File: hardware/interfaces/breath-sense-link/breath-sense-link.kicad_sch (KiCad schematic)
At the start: 5 parts

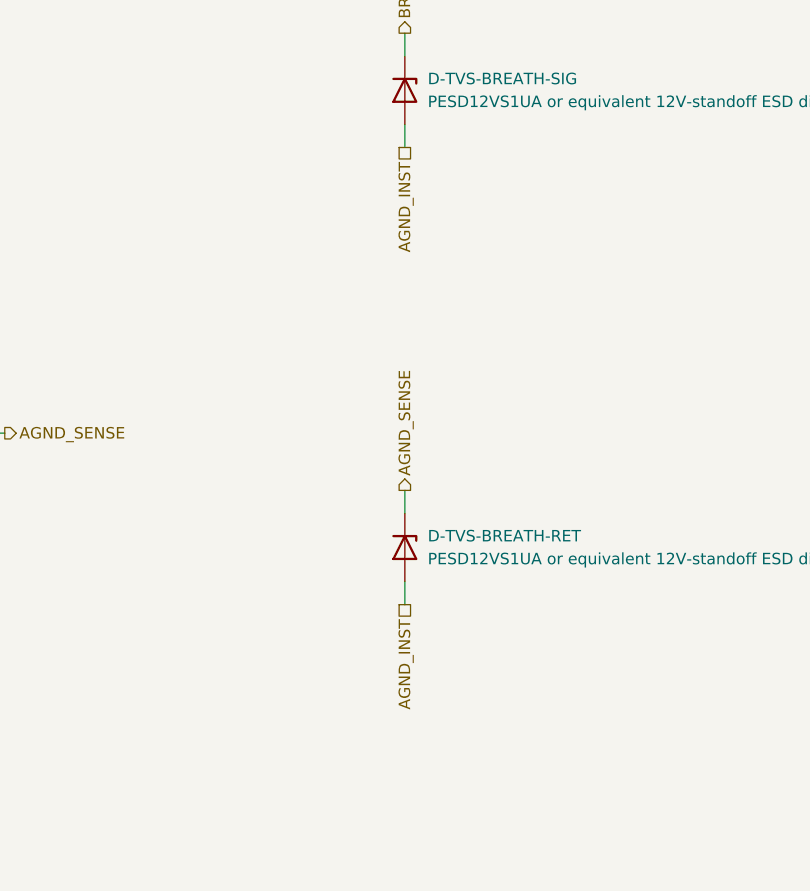
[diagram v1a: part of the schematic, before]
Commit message: Four-layer main-board ground written; breath clamps to the PWR_GND plane
power-entry-instrument.md section 2: layer 2 is the PWR_GND plane under every
SPI/chain/LED trace; AGND_INST is an island under the analog block, tied by
NT-AGND under U-ADC; the breath pair crosses as a pair (AGND_SENSE Kelvin at
the sensor). D-TVS-BREATH anodes move from AGND_INST to PWR_GND (sheet, board,
nets.yaml). dig-gnd-topology stays disputed: its dispute is the MODULE board,
whose layer count is the owner's; a four-layer proposal is recorded on it.

Co-Authored-By: Claude Opus 5.5 <noreply@anthropic.com>
Claude-Session: https://claude.ai/code/session_01LmB4muFXnoLprWX4JzuJ5A
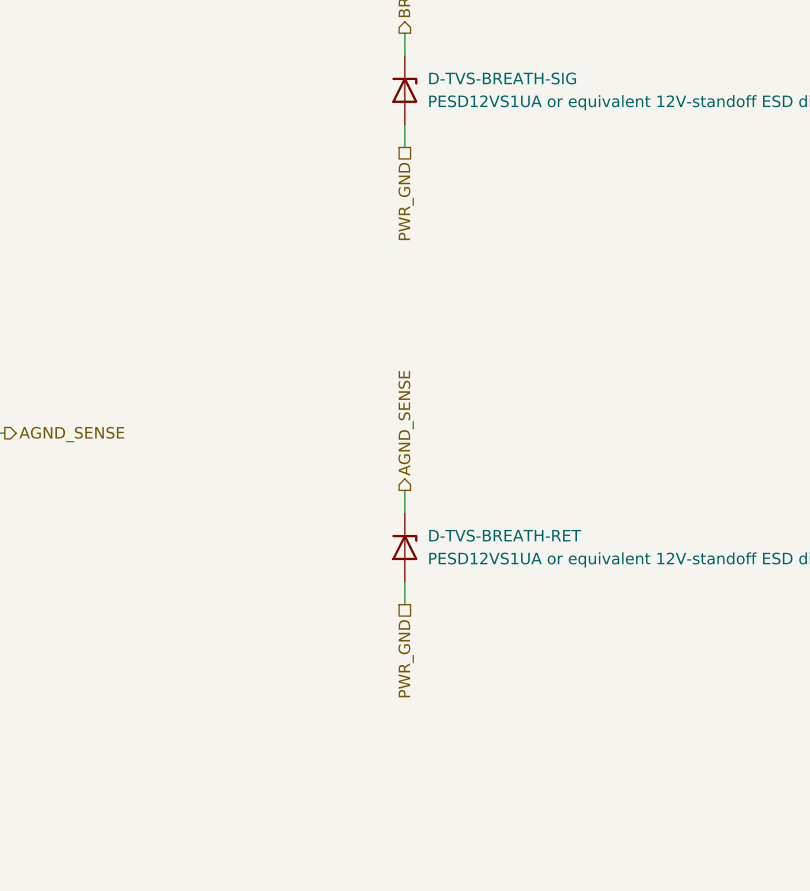
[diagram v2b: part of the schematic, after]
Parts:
- D-TVS-BREATH-RET: Note The second of the pair, on the AGND conductor -> The second of the pair, on the AGND_SENSE conductor. Anode 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
- D-TVS-BREATH-SIG: Note AT THE CONNECTOR, 12 V standoff - above the sensor's full scale so it never conducts in play -> AT THE CONNECTOR, 12 V standoff - above the sensor's full scale so it never conducts in play. Anode to the PWR_GND plane at J-UMB, never to the analog island
- R1b: Note THE TWIN IN THE AGND LEG, and it was missing until 2026-09-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 -> THE TWIN IN THE AGND_SENSE LEG. Without it the return is no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
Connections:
- net AGND_INST: no longer D-TVS-BREATH-RET.2 (A), D-TVS-BREATH-SIG.2 (A)
- new net PWR_GND: D-TVS-BREATH-RET.2 (A), D-TVS-BREATH-SIG.2 (A)
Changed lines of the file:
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@@
     (property "Row" "R-SER-BREATH-INST" (at 139.7 139.7 0) (effects (font (size 1.27 1.27)) hide))
     (property "Pins" "1=1 2=2" (at 139.7 139.7 0) (effects (font (size 1.27 1.27)) hide))
-    (property "Note" "THE TWIN IN THE AGND LEG, and it was missing until 2026-09-21. Without it the return is not matched to the signal leg and the link's CMRR is set by that asymmetry rather than by the in-amp" (at 139.7 139.7 0) (effects (font (size 1.27 1.27)) hide))
+    (property "Note" "THE TWIN IN THE AGND_SENSE LEG. Without it the return is not matched to the signal leg and the link's CMRR is set by that asymmetry rather than by the in-amp. Its AGND_INST end is a trace of its own from U-BREATH pin 3 (breath-sense-link.md, Where it sits)" (at 139.7 139.7 0) (effects (font (size 1.27 1.27)) hide))
     (property "Manufacturer" "UNI-ROYAL" (at 139.7 139.7 0) (effects (font (size 1.27 1.27)) hide))
     (property "MPN" "1206W4F1001T5E" (at 139.7 139.7 0) (effects (font (size 1.27 1.27)) hide))
@@
     (property "Pins" "A=2(A) K=1(K)" (at 190.5 101.6 0) (effects (font (size 1.27 1.27)) hide))
     (property "Drawn_as" "D-TVS-BREATH" (at 190.5 101.6 0) (effects (font (size 1.27 1.27)) hide))
-    (property "Note" "AT THE CONNECTOR, 12 V standoff - above the sensor's full scale so it never conducts in play" (at 190.5 101.6 0) (effects (font (size 1.27 1.27)) hide))
+    (property "Note" "AT THE CONNECTOR, 12 V standoff - above the sensor's full scale so it never conducts in play. Anode to the PWR_GND plane at J-UMB, never to the analog island" (at 190.5 101.6 0) (effects (font (size 1.27 1.27)) hide))
     (property "Pins_source" "KiCad's diode convention: 1 cathode, 2 anode; a unidirectional ESD diode" (at 190.5 101.6 0) (effects (font (size 1.27 1.27)) hide))
     (property "Manufacturer" "Nexperia" (at 190.5 101.6 0) (effects (font (size 1.27 1.27)) hide))
@@
     (property "Row" "D-TVS-BREATH" (at 190.5 152.4 0) (effects (font (size 1.27 1.27)) hide))
     (property "Pins" "A=2(A) K=1(K)" (at 190.5 152.4 0) (effects (font (size 1.27 1.27)) hide))
-    (property "Note" "The second of the pair, on the AGND conductor" (at 190.5 152.4 0) (effects (font (size 1.27 1.27)) hide))
+    (property "Note" "The second of the pair, on the AGND_SENSE conductor. Anode to the PWR_GND plane at J-UMB, never to the analog island" (at 190.5 152.4 0) (effects (font (size 1.27 1.27)) hide))
     (property "Pins_source" "KiCad's diode convention: 1 cathode, 2 anode; a unidirectional ESD diode" (at 190.5 152.4 0) (effects (font (size 1.27 1.27)) hide))
     (property "Manufacturer" "Nexperia" (at 190.5 152.4 0) (effects (font (size 1.27 1.27)) hide))
@@
     (property "From" "carrier/power-entry-instrument" (at 76.2 111.76 0) (effects (font (size 1.27 1.27)) hide)))
   (wire (pts (xy 190.5 105.41) (xy 190.5 107.95)) (stroke (width 0) (type default)))
-  (hierarchical_label "AGND_INST" (shape passive) (at 190.5 107.95 270) (effects (font (size 1.27 1.27)) (justify right))
+  (hierarchical_label "PWR_GND" (shape passive) (at 190.5 107.95 270) (effects (font (size 1.27 1.27)) (justify right))
     (property "Dir" "ref" (at 190.5 107.95 0) (effects (font (size 1.27 1.27)) hide))
-    (property "From" "carrier/power-entry-instrument" (at 190.5 107.95 0) (effects (font (size 1.27 1.27)) hide)))
+    (property "From" "module/power-entry" (at 190.5 107.95 0) (effects (font (size 1.27 1.27)) hide)))
   (wire (pts (xy 190.5 156.21) (xy 190.5 158.75)) (stroke (width 0) (type default)))
-  (hierarchical_label "AGND_INST" (shape passive) (at 190.5 158.75 270) (effects (font (size 1.27 1.27)) (justify right))
+  (hierarchical_label "PWR_GND" (shape passive) (at 190.5 158.75 270) (effects (font (size 1.27 1.27)) (justify right))
     (property "Dir" "ref" (at 190.5 158.75 0) (effects (font (size 1.27 1.27)) hide))
-    (property "From" "carrier/power-entry-instrument" (at 190.5 158.75 0) (effects (font (size 1.27 1.27)) hide)))
+    (property "From" "module/power-entry" (at 190.5 158.75 0) (effects (font (size 1.27 1.27)) hide)))
   (text "The instrument end of the breath link: every part here is on the main board. The umbilical conductors BREATH_SENSE and AGND_SENSE continue on interfaces/spi-link (J-UMB pins 1 and 2);\nthe module end (R-SER-BREATH, the in-amp) is module/breath-receive-stage. Which board carries which part: breath-sense-link.md, 'Which board places what'." (at 25.4 25.4 0) (effects (font (size 1.27 1.27)) (justify left top)))
   (text "FROM THE HAND-WRITTEN NETLIST THIS SHEET REPLACES (the part notes are on each part's Note field):\n\nAUTHORITATIVE for connectivity. THE DRAWING IS ON ANOTHER PAGE - carrier.md §2 - and the module half of this link is\ndrawn again on module/breath-receive-stage, which declares these same parts `foreign:` because the pole and the CMRR\nbudget are derived there.\n\nR-SER-BREATH IS NOT HERE. The 10k 0.1% pair is the MODULE-side series protection and module/breath-receive-stage places\nit; this circuit's rows are the instrument-side 1k pair and the sensor." (at 25.4 190.5 0) (effects (font (size 1.27 1.27)) (justify left top)))

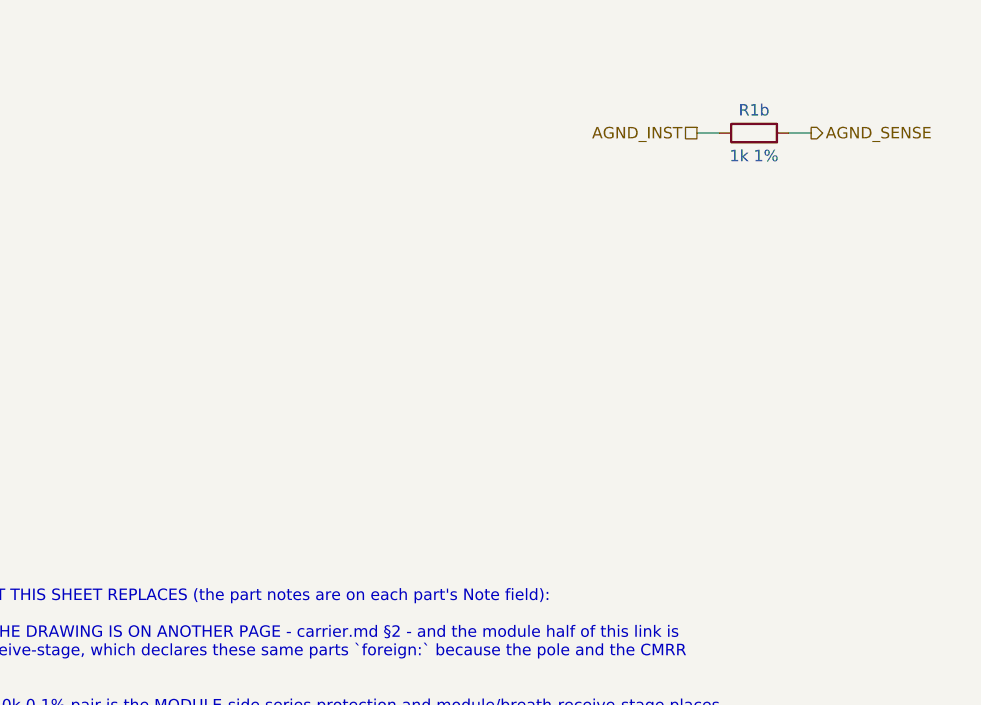
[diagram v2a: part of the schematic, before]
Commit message: Sensor Figure 3 capacitors and U-BUF bypass drawn; VS load simulated as built; F1 verification ledger
C-SENSOR-VS-BULK/-HF and C-SENSOR-OUT at U-BREATH (owner, A1-5), C-DEC-BUF at
U-BUF V+ (A8-1); excitation sims load VS with everything netlisted there.
VERIFIED-F1.md closes every A1 id and A8-1/A8-4, with A1-1's options for the owner.

Co-Authored-By: Claude Opus 5.5 <noreply@anthropic.com>
Claude-Session: https://claude.ai/code/session_01LmB4muFXnoLprWX4JzuJ5A
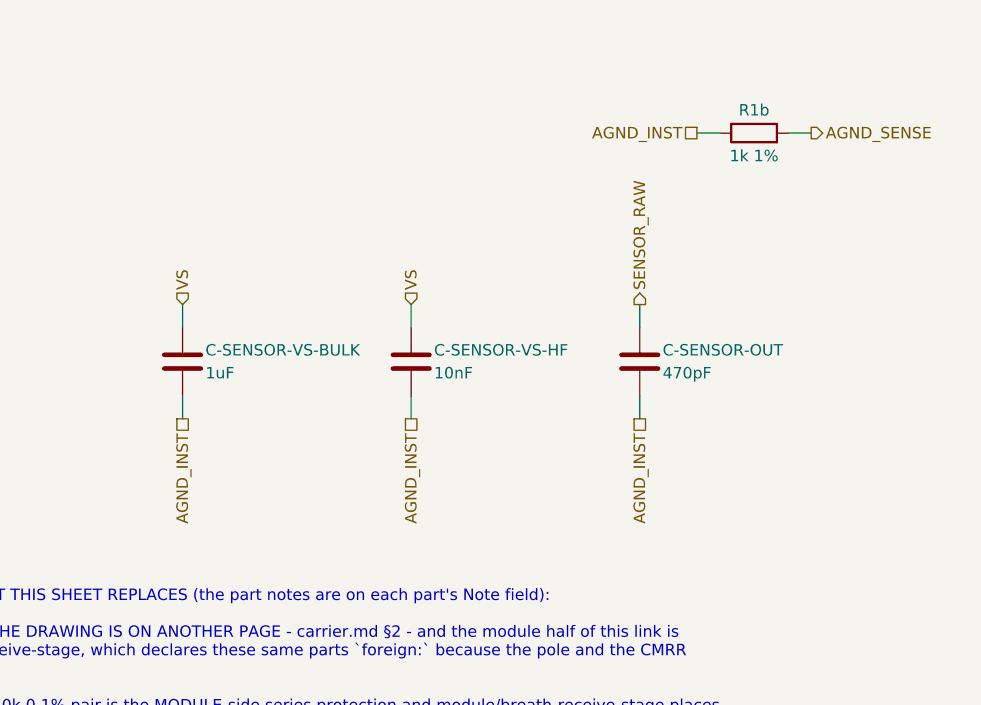
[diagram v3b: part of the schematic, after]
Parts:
- added C-SENSOR-OUT: 470pF, Capacitor_SMD:C_0805_2012Metric, symbol Device:C
- added C-SENSOR-VS-BULK: 1uF, Capacitor_SMD:C_0805_2012Metric, symbol Device:C
- added C-SENSOR-VS-HF: 10nF, Capacitor_SMD:C_0805_2012Metric, symbol Device:C
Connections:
- net AGND_INST: now also C-SENSOR-OUT.2, C-SENSOR-VS-BULK.2, C-SENSOR-VS-HF.2
- net SENSOR_RAW: now also C-SENSOR-OUT.1
- net VS: now also C-SENSOR-VS-BULK.1, C-SENSOR-VS-HF.1
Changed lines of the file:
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@@
   (text "The instrument end of the breath link: every part here is on the main board. The umbilical conductors BREATH_SENSE and AGND_SENSE continue on interfaces/spi-link (J-UMB pins 1 and 2);\nthe module end (R-SER-BREATH, the in-amp) is module/breath-receive-stage. Which board carries which part: breath-sense-link.md, 'Which board places what'." (at 25.4 25.4 0) (effects (font (size 1.27 1.27)) (justify left top)))
   (text "FROM THE HAND-WRITTEN NETLIST THIS SHEET REPLACES (the part notes are on each part's Note field):\n\nAUTHORITATIVE for connectivity. THE DRAWING IS ON ANOTHER PAGE - carrier.md §2 - and the module half of this link is\ndrawn again on module/breath-receive-stage, which declares these same parts `foreign:` because the pole and the CMRR\nbudget are derived there.\n\nR-SER-BREATH IS NOT HERE. The 10k 0.1% pair is the MODULE-side series protection and module/breath-receive-stage places\nit; this circuit's rows are the instrument-side 1k pair and the sensor." (at 25.4 190.5 0) (effects (font (size 1.27 1.27)) (justify left top)))
+  (symbol (lib_id "Device:C") (at 76.2 165.1 0) (unit 1)
+    (in_bom yes) (on_board yes) (dnp no)
+    (property "Reference" "C-SENSOR-VS-BULK" (at 78.74000000000001 163.82999999999998 0) (effects (font (size 1.27 1.27)) (justify left)))
+    (property "Value" "1uF" (at 78.74000000000001 166.37 0) (effects (font (size 1.27 1.27)) (justify left)))
+    (property "Footprint" "Capacitor_SMD:C_0805_2012Metric" (at 76.2 165.1 0) (effects (font (size 1.27 1.27)) hide))
+    (property "Datasheet" "" (at 76.2 165.1 0) (effects (font (size 1.27 1.27)) hide))
+    (property "Row" "C-SENSOR-VS-BULK" (at 76.2 165.1 0) (effects (font (size 1.27 1.27)) hide))
+    (property "Pins" "1=1 2=2" (at 76.2 165.1 0) (effects (font (size 1.27 1.27)) hide))
+    (property "Note" "NXP's Figure 3 decoupling, 1.0 uF on VS: AT U-BREATH pin 2, returning to pin 3's AGND_INST (owner, 2026-10-01, A1-5) [ds datasheets/analog/MPXV4006DP.pdf p.5, Figure 3]" (at 76.2 165.1 0) (effects (font (size 1.27 1.27)) hide))
+    (property "Manufacturer" "Samsung Electro-Mechanics" (at 76.2 165.1 0) (effects (font (size 1.27 1.27)) hide))
+    (property "MPN" "CL21B105KBFNNNE" (at 76.2 165.1 0) (effects (font (size 1.27 1.27)) hide))
+    (property "LCSC" "C28323" (at 76.2 165.1 0) (effects (font (size 1.27 1.27)) hide))
+    (property "Assembly" "machine" (at 76.2 165.1 0) (effects (font (size 1.27 1.27)) hide))
+    (pin "1")
+    (pin "2")
+    (instances (project "main-board" (path "/b12a49ac-ffa0-5078-b2ba-e15d161f1936/5b7e1c1a-2f0b-5a3c-9d6e-b5e0a1c2d301" (reference "C201") (unit 1))) (project "breath-sense-link" (path "/389f5e80-1343-55c9-9647-41a2f4e558a0" (reference "C-SENSOR-VS-BULK") (unit 1))))
+  )
+  (wire (pts (xy 76.2 161.29) (xy 76.2 158.75)) (stroke (width 0) (type default)))
+  (hierarchical_label "VS" (shape input) (at 76.2 158.75 90) (effects (font (size 1.27 1.27)) (justify left))
+    (property "Dir" "in" (at 76.2 158.75 0) (effects (font (size 1.27 1.27)) hide))
+    (property "From" "carrier/breath-excitation-reference" (at 76.2 158.75 0) (effects (font (size 1.27 1.27)) hide))
+    (property "Figure" "riso-ref-topology" (at 76.2 158.75 0) (effects (font (size 1.27 1.27)) hide)))
+  (wire (pts (xy 76.2 168.91) (xy 76.2 171.45)) (stroke (width 0) (type default)))
+  (hierarchical_label "AGND_INST" (shape passive) (at 76.2 171.45 270) (effects (font (size 1.27 1.27)) (justify right))
+    (property "Dir" "ref" (at 76.2 171.45 0) (effects (font (size 1.27 1.27)) hide))
+    (property "From" "carrier/power-entry-instrument" (at 76.2 171.45 0) (effects (font (size 1.27 1.27)) hide)))
+  (symbol (lib_id "Device:C") (at 101.6 165.1 0) (unit 1)
+    (in_bom yes) (on_board yes) (dnp no)
+    (property "Reference" "C-SENSOR-VS-HF" (at 104.14 163.82999999999998 0) (effects (font (size 1.27 1.27)) (justify left)))
+    (property "Value" "10nF" (at 104.14 166.37 0) (effects (font (size 1.27 1.27)) (justify left)))
+    (property "Footprint" "Capacitor_SMD:C_0805_2012Metric" (at 101.6 165.1 0) (effects (font (size 1.27 1.27)) hide))
+    (property "Datasheet" "" (at 101.6 165.1 0) (effects (font (size 1.27 1.27)) hide))
+    (property "Row" "C-SENSOR-VS-HF" (at 101.6 165.1 0) (effects (font (size 1.27 1.27)) hide))
+    (property "Pins" "1=1 2=2" (at 101.6 165.1 0) (effects (font (size 1.27 1.27)) hide))
+    (property "Note" "NXP's Figure 3 decoupling, 0.01 uF on VS, beside C-SENSOR-VS-BULK at U-BREATH pin 2 [ds datasheets/analog/MPXV4006DP.pdf p.5, Figure 3]" (at 101.6 165.1 0) (effects (font (size 1.27 1.27)) hide))
+    (property "Manufacturer" "Samsung Electro-Mechanics" (at 101.6 165.1 0) (effects (font (size 1.27 1.27)) hide))
+    (property "MPN" "CL21C103JBFNNNE" (at 101.6 165.1 0) (effects (font (size 1.27 1.27)) hide))
+    (property "LCSC" "C27071" (at 101.6 165.1 0) (effects (font (size 1.27 1.27)) hide))
+    (property "Assembly" "machine" (at 101.6 165.1 0) (effects (font (size 1.27 1.27)) hide))
+    (pin "1")
+    (pin "2")
+    (instances (project "main-board" (path "/b12a49ac-ffa0-5078-b2ba-e15d161f1936/5b7e1c1a-2f0b-5a3c-9d6e-b5e0a1c2d301" (reference "C202") (unit 1))) (project "breath-sense-link" (path "/389f5e80-1343-55c9-9647-41a2f4e558a0" (reference "C-SENSOR-VS-HF") (unit 1))))
+  )
+  (wire (pts (xy 101.6 161.29) (xy 101.6 158.75)) (stroke (width 0) (type default)))
+  (hierarchical_label "VS" (shape input) (at 101.6 158.75 90) (effects (font (size 1.27 1.27)) (justify left))
+    (property "Dir" "in" (at 101.6 158.75 0) (effects (font (size 1.27 1.27)) hide))
+    (property "From" "carrier/breath-excitation-reference" (at 101.6 158.75 0) (effects (font (size 1.27 1.27)) hide))
+    (property "Figure" "riso-ref-topology" (at 101.6 158.75 0) (effects (font (size 1.27 1.27)) hide)))
+  (wire (pts (xy 101.6 168.91) (xy 101.6 171.45)) (stroke (width 0) (type default)))
+  (hierarchical_label "AGND_INST" (shape passive) (at 101.6 171.45 270) (effects (font (size 1.27 1.27)) (justify right))
+    (property "Dir" "ref" (at 101.6 171.45 0) (effects (font (size 1.27 1.27)) hide))
+    (property "From" "carrier/power-entry-instrument" (at 101.6 171.45 0) (effects (font (size 1.27 1.27)) hide)))
+  (symbol (lib_id "Device:C") (at 127.0 165.1 0) (unit 1)
+    (in_bom yes) (on_board yes) (dnp no)
+    (property "Reference" "C-SENSOR-OUT" (at 129.54 163.82999999999998 0) (effects (font (size 1.27 1.27)) (justify left)))
+    (property "Value" "470pF" (at 129.54 166.37 0) (effects (font (size 1.27 1.27)) (justify left)))
+    (property "Footprint" "Capacitor_SMD:C_0805_2012Metric" (at 127.0 165.1 0) (effects (font (size 1.27 1.27)) hide))
+    (property "Datasheet" "" (at 127.0 165.1 0) (effects (font (size 1.27 1.27)) hide))
+    (property "Row" "C-SENSOR-OUT" (at 127.0 165.1 0) (effects (font (size 1.27 1.27)) hide))
+    (property "Pins" "1=1 2=2" (at 127.0 165.1 0) (effects (font (size 1.27 1.27)) hide))
+    (property "Note" "NXP's Figure 3 output capacitor, 470 pF on Vout: at U-BREATH pin 4, ahead of U-BUF B's input, so neither the link nor the ADC sees it [ds datasheets/analog/MPXV4006DP.pdf p.5, Figure 3]" (at 127.0 165.1 0) (effects (font (size 1.27 1.27)) hide))
+    (property "Manufacturer" "YAGEO" (at 127.0 165.1 0) (effects (font (size 1.27 1.27)) hide))
+    (property "MPN" "CC0805JRNPOYBN471" (at 127.0 165.1 0) (effects (font (size 1.27 1.27)) hide))
+    (property "LCSC" "C277525" (at 127.0 165.1 0) (effects (font (size 1.27 1.27)) hide))
+    (property "Assembly" "machine" (at 127.0 165.1 0) (effects (font (size 1.27 1.27)) hide))
+    (pin "1")
+    (pin "2")
+    (instances (project "main-board" (path "/b12a49ac-ffa0-5078-b2ba-e15d161f1936/5b7e1c1a-2f0b-5a3c-9d6e-b5e0a1c2d301" (reference "C203") (unit 1))) (project "breath-sense-link" (path "/389f5e80-1343-55c9-9647-41a2f4e558a0" (reference "C-SENSOR-OUT") (unit 1))))
+  )
+  (wire (pts (xy 127.0 161.29) (xy 127.0 158.75)) (stroke (width 0) (type default)))
+  (hierarchical_label "SENSOR_RAW" (shape output) (at 127.0 158.75 90) (effects (font (size 1.27 1.27)) (justify left))
+    (property "Dir" "out" (at 127.0 158.75 0) (effects (font (size 1.27 1.27)) hide))
+    (property "To" "carrier/breath-excitation-reference" (at 127.0 158.75 0) (effects (font (size 1.27 1.27)) hide))
+    (property "Figure" "sensor-full-scale" (at 127.0 158.75 0) (effects (font (size 1.27 1.27)) hide)))
+  (wire (pts (xy 127.0 168.91) (xy 127.0 171.45)) (stroke (width 0) (type default)))
+  (hierarchical_label "AGND_INST" (shape passive) (at 127.0 171.45 270) (effects (font (size 1.27 1.27)) (justify right))
+    (property "Dir" "ref" (at 127.0 171.45 0) (effects (font (size 1.27 1.27)) hide))
+    (property "From" "carrier/power-entry-instrument" (at 127.0 171.45 0) (effects (font (size 1.27 1.27)) hide)))
   (sheet_instances (path "/" (page "1")))
 )
